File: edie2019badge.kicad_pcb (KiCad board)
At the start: 2 copper layers, 90 x 95.7 mm, 93 parts, among them CN1 USB-Micro, CN2 2x2, CN3 2x2, CN4 2x2, IC1 ESP-32-WROOM, IC2 XC6206P332MR, IC3 TP4056, IC4 DW01, IC5 FT230XS, SW1 switch_3x4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

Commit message: added more logos
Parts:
- added G***: LOGO, logos:nakkiservo, B.Cu at (125.6, 108.0)
- added G***: LOGO, logos:netl, B.Cu at (74.0, 97.0)
- added G***: LOGO, logos:hacklabfi, B.Cu at (98.8, 134.8)
- moved G*** 28.0 mm to (77.8, 74.2)

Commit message: added game crew logo
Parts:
- added G***: LOGO, logos:disobey, B.Cu at (108.8, 95.4)
- added G***: LOGO, logos:edgc, B.Cu at (86.0, 110.5)
- moved G*** 49.7 mm to (117.6, 73.2)
- moved G*** 5.37 mm to (82.6, 76.6)
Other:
- board text added: "- - - -=greets=- - - -"

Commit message: did led strip decoupling capacitor routing
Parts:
- turned C5 to 180 degrees
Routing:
- net GND: track 773.9 -> 783.1 mm, vias 24 -> 30
- net /LED strip/+V_LEDs: track 548.5 -> 556.7 mm, vias 7 -> 12
- net /esp32/battery_charging: track 83.9 -> 85.0 mm, vias 2 -> 3

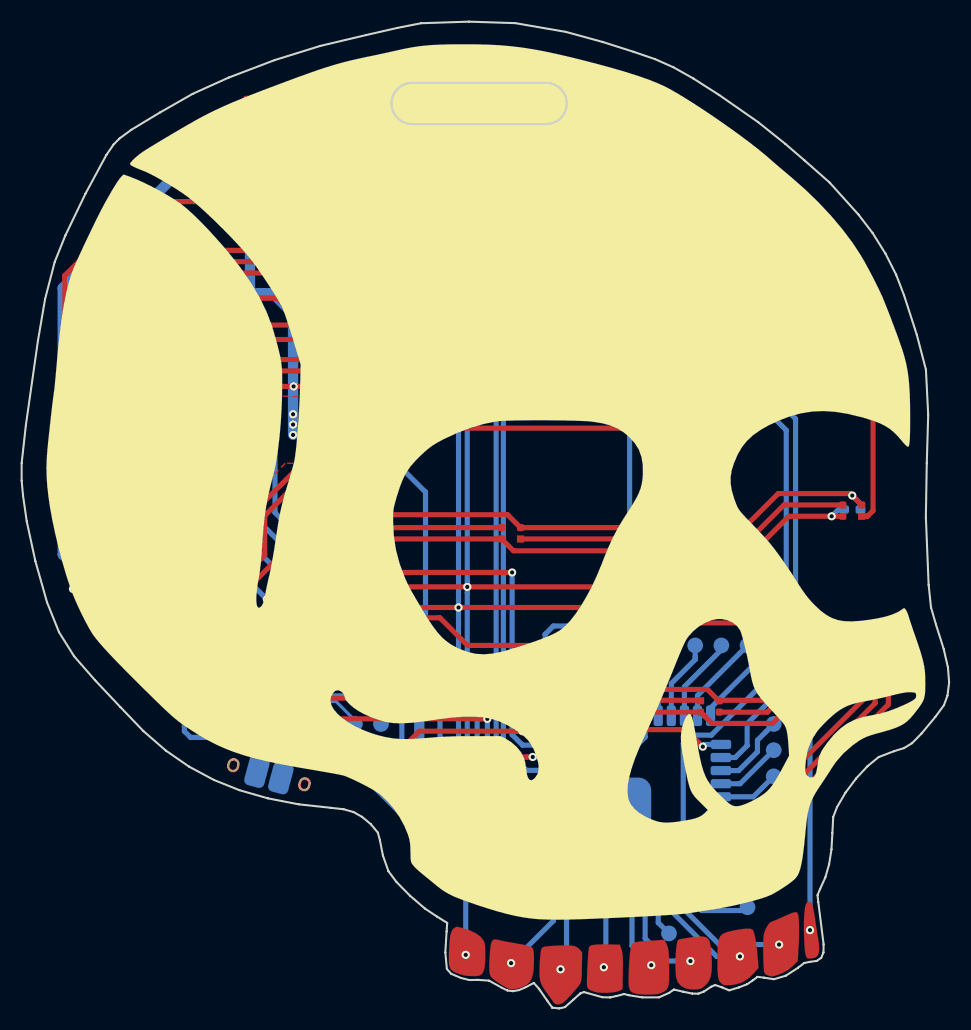
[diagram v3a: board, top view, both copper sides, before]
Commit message: added bypass capacitors to most of the leds, reworked layout
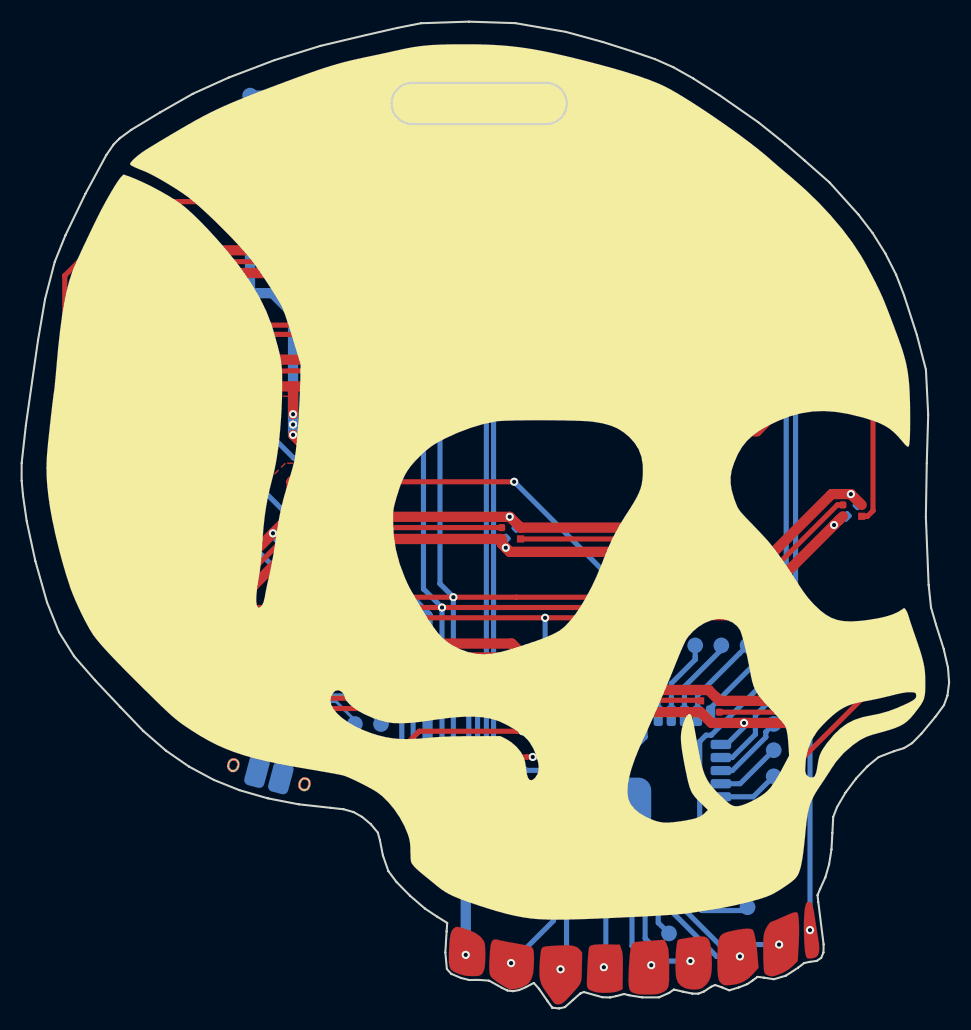
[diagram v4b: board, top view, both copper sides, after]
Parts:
- removed C5: C, SMT:0603
- added C14: C, SMT:0603, B.Cu at (95.5, 109.8)
- added C15: C, SMT:0603, B.Cu at (80.6, 107.0)
- added C16: C, SMT:0603, B.Cu at (63.4, 111.6)
- added C17: C, SMT:0603, B.Cu at (55.0, 100.5)
- added C18: C, SMT:0603, B.Cu at (76.0, 91.5)
- added C19: C, SMT:0603, B.Cu at (93.9, 95.8)
- added C20: C, SMT:0603, B.Cu at (112.4, 99.0)
- added C21: C, SMT:0603, B.Cu at (127.0, 93.6)
- added C22: C, SMT:0603, B.Cu at (126.9, 77.1)
- added C23: C, SMT:0603, B.Cu at (112.1, 84.3)
- added C24: C, SMT:0603, B.Cu at (89.5, 81.0)
- added C25: C, SMT:0603, B.Cu at (68.0, 79.5)
- added C26: C, SMT:0603, B.Cu at (52.5, 86.0)
- added C27: C, SMT:0603, B.Cu at (55.5, 68.9)
- added C28: C, SMT:0603, B.Cu at (78.5, 70.0)
- added C29: C, SMT:0603, B.Cu at (105.5, 72.0)
- added C30: C, SMT:0603, B.Cu at (92.0, 63.0)
- added C31: C, SMT:0603, B.Cu at (71.5, 55.1)
- added R13: R, SMT:0603, B.Cu at (56.0, 89.2)
- moved C6 35.3 mm to (117.1, 127.4), turned to 45 degrees
- moved TP18 3.59 mm to (68.6, 53.3)
- moved TP19 3.59 mm to (68.6, 58.4)
- moved C12 0.20 mm to (66.2, 111.6)
- moved C4 0.20 mm to (119.5, 65.7), turned to 45 degrees
- moved C7 0.20 mm to (128.3, 108.5), turned to 225 degrees
- turned C3 to 225 degrees
- turned C8 to 45 degrees
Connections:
- net /esp32/battery_charging renamed /esp32/~battery_charging
- IC3 pad 6: Net-(IC3-Pad6) -> /esp32/~battery_standby
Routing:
- net GND: track 783.1 -> 615.5 mm, vias 30 -> 42
- net /LED strip/+V_LEDs: track 556.7 -> 490.2 mm, vias 12 -> 28
- net +5V_USB: track 100.4 -> 84.3 mm
- net /esp32/~battery_charging: track 85.0 -> 74.8 mm, vias 3 -> 2
- net /esp32/SCL: track 147.0 -> 153.9 mm, vias 4 -> 5
- net +3V3: track 187.2 -> 181.4 mm
- net /esp32/SDA: track 142.9 -> 148.2 mm
- net Net-(IC1-Pad23): track 66.2 -> 61.9 mm
- net /esp32/~battery_standby: track 0.00 -> 1.98 mm
- net /USB interface/TX: track 44.1 -> 45.8 mm
- net Net-(C12-Pad1): track 28.2 -> 27.0 mm
- net Net-(IC1-Pad16): track 74.1 -> 75.1 mm
- net Net-(D20-Pad1): track 27.7 -> 27.0 mm
- net /LED strip/LED_strip_enable: track 101.7 -> 102.3 mm
- net VCC: track 32.3 -> 32.8 mm

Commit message: layout complete. changed NTC package to 0805
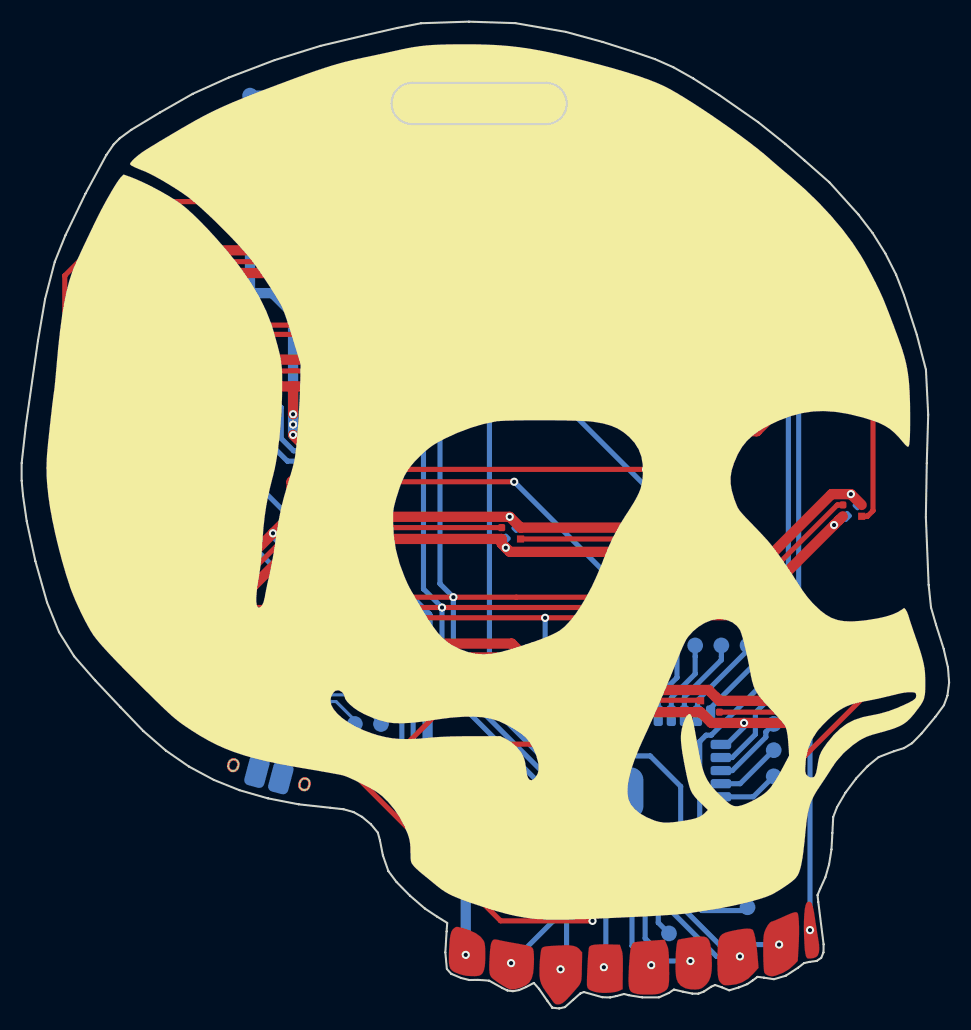
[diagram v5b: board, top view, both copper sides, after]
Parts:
- removed TP10: test_point, PCB:test_point
- R10: footprint SMT:0603 -> SMT:0805
- moved R8 2.30 mm to (63.8, 84.6)
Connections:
- net Net-(IC1-Pad16) renamed /esp32/button_mid
- net Net-(IC1-Pad23) renamed /esp32/button_right
- net Net-(IC1-Pad25) renamed /esp32/button_left
- IC1 pad 10: Net-(IC1-Pad10) -> /esp32/~battery_standby
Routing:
- net /esp32/~battery_standby: track 1.98 -> 95.8 mm, vias 0 -> 4
- net /LED strip/LED_strip_enable: track 102.3 -> 88.0 mm
- net Net-(T3-Pad1): track 0.00 -> 7.31 mm, vias 0 -> 2
- net Net-(IC1-Pad10): track 7.25 -> 0.00 mm
- net /USB interface/TX: track 45.8 -> 42.3 mm
- net /USB interface/USB_power: track 27.5 -> 30.3 mm
- net Net-(IC3-Pad1): track 7.60 -> 5.26 mm
- net GND: track 615.5 -> 613.2 mm, vias 42 -> 44
- net +3V3: track 181.4 -> 182.6 mm
- net /esp32/button_left: track 101.9 -> 103.1 mm
- net VCC: track 32.8 -> 33.7 mm
- net /LED strip/LED_strip_data: track 24.5 -> 23.7 mm

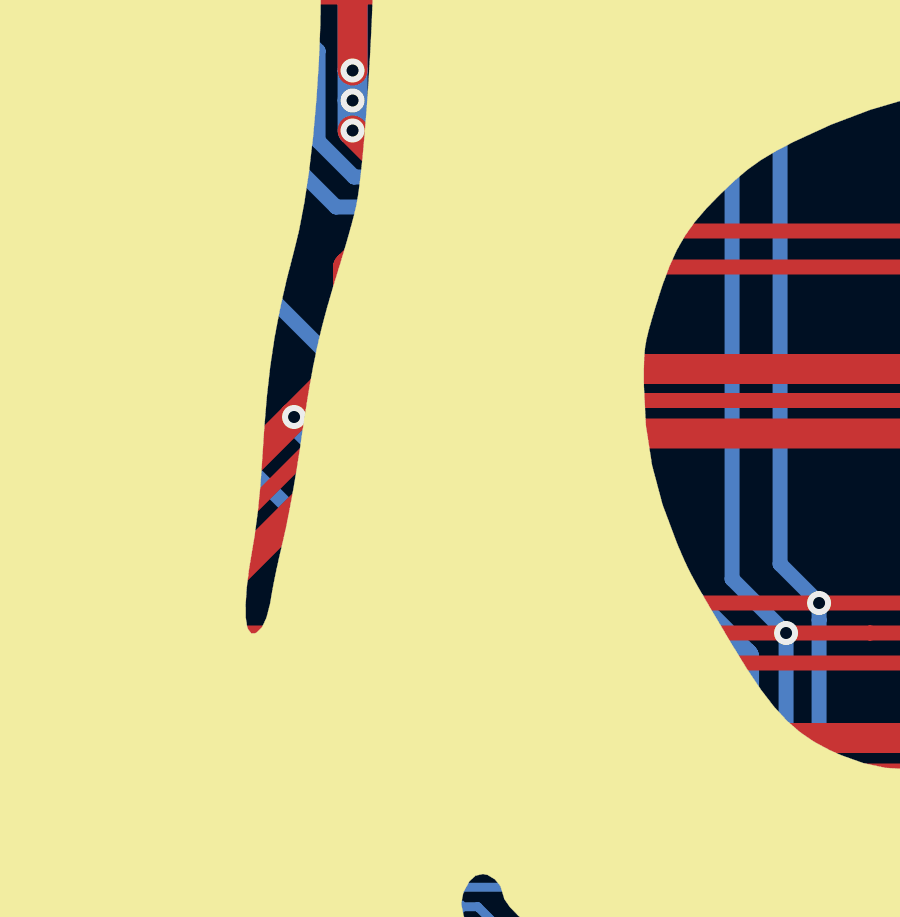
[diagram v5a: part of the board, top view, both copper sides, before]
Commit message: tweaked branding
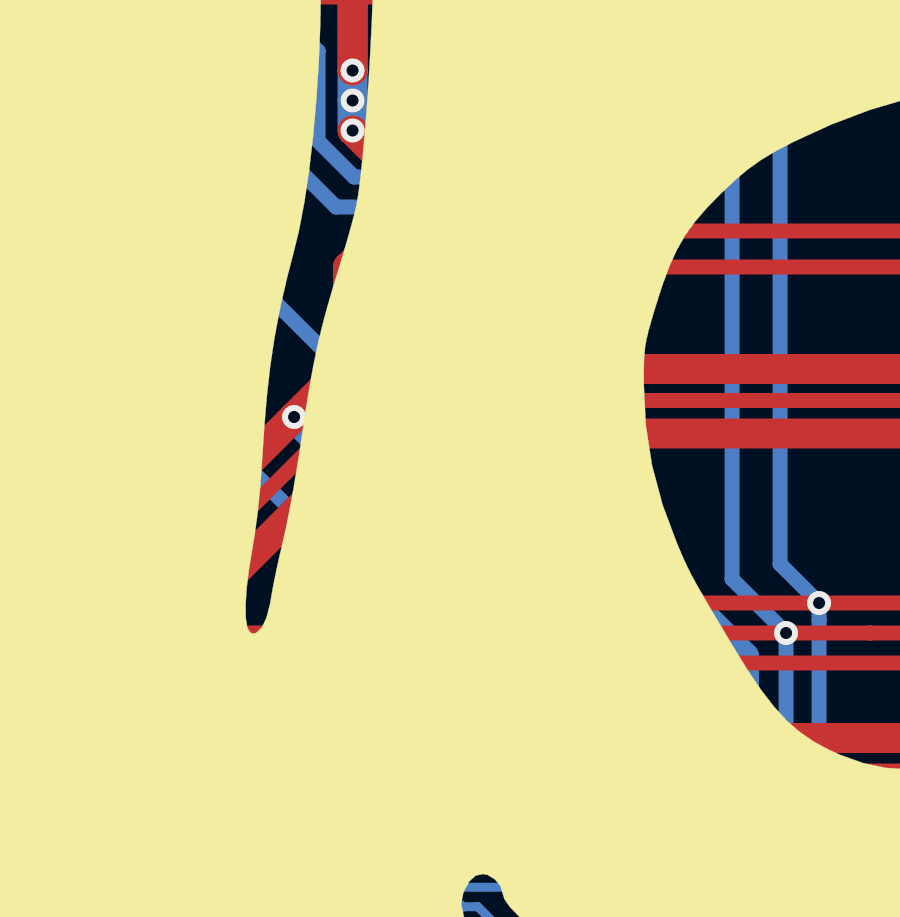
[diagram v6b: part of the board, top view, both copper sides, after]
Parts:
- removed the G*** at (108.8, 95.4)
- moved G*** 41.2 mm to (78.6, 86.4)
- moved G*** 24.8 mm to (62.2, 103.6)
- moved G*** 21.9 mm to (101.8, 87.2)
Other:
- board text removed: "- - - -=greets=- - - -"

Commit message: added pull-down for led power signal
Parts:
- added R14: R, SMT:0603, B.Cu at (53.0, 73.8)
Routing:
- net /LED strip/LED_strip_enable: track 88.0 -> 89.0 mm
